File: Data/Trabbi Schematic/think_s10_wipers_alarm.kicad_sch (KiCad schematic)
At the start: 7 parts, among them K1 Wiper Relay R1, K2 Tailgate Release Relay R13, M1 Wiper Motor (E19), M2 Washer Pump (E10), SW1 Wiper Switch (C26), U1 Alarm Control Unit (P4)

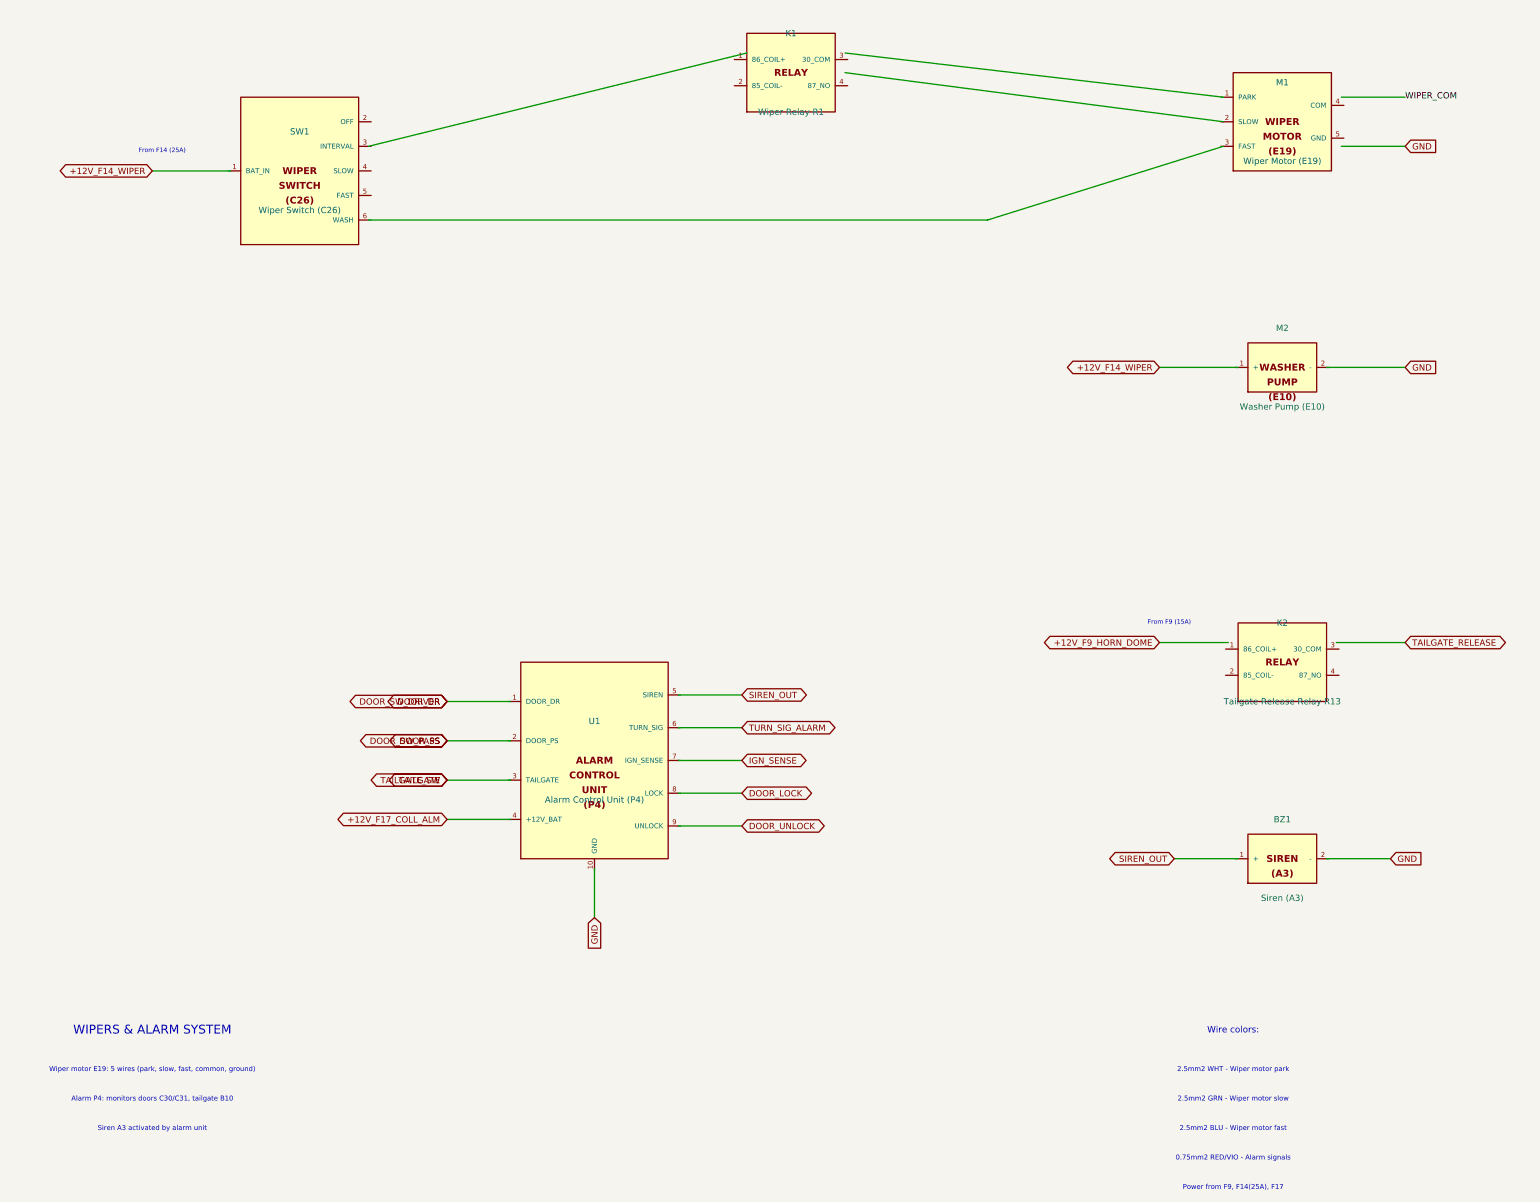
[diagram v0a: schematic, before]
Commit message: Fix wire-to-pin connections: use exact calculated pin positions
Refactored gen_think_complete.py to compute exact pin schematic
coordinates instead of using approximate manual offsets. Added p()
method to Sheet class that transforms symbol-local pin positions to
schematic coordinates. All 232 wire calls across 13 sub-sheet
generators now use p() for pin endpoints, fixing misaligned
connections (previously off by 0.54-10+ units).

Co-Authored-By: Claude Opus 4.6 <noreply@anthropic.com>
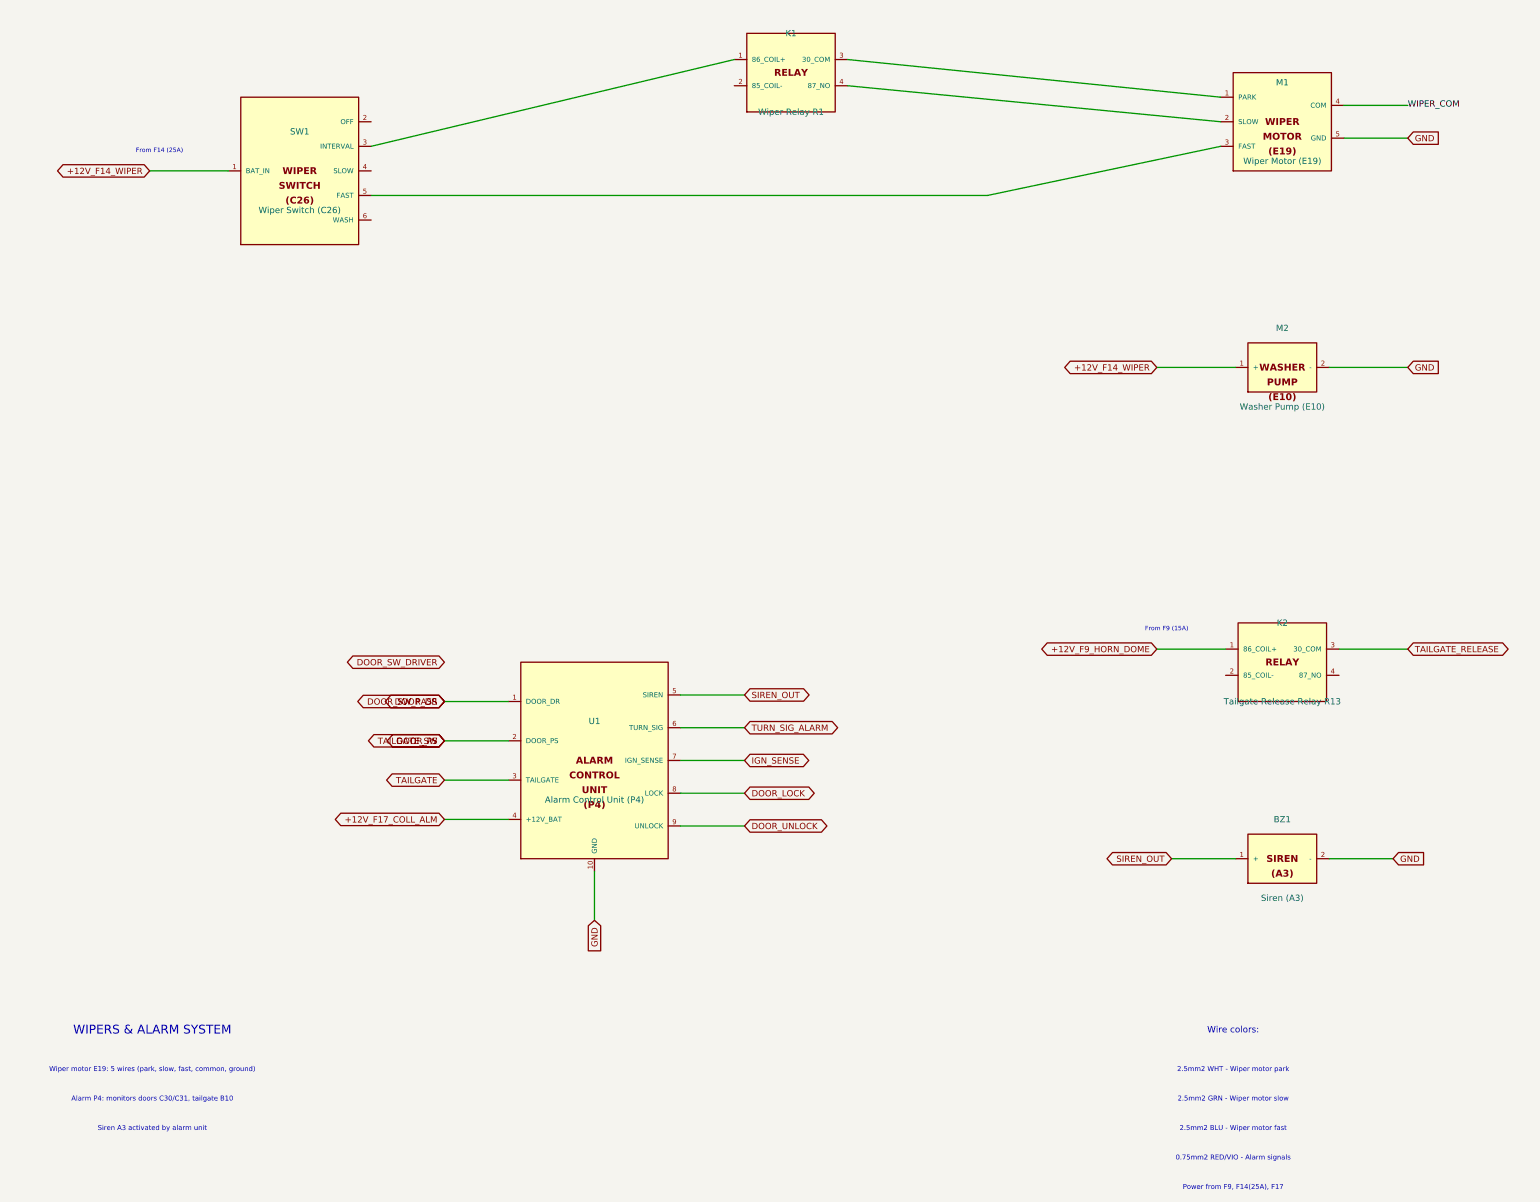
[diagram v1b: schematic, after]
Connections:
- net +12V_F14_WIPER: now also M2.1 (+), SW1.1 (BAT_IN)
- net +12V_F17_COLL_ALM: now also U1.4 (+12V_BAT)
- net +12V_F9_HORN_DOME: now also K2.1 (86_COIL+)
- net DOOR_DR: now also U1.1 (DOOR_DR)
- net DOOR_LOCK: now also U1.8 (LOCK)
- net DOOR_PS: now also U1.2 (DOOR_PS)
- net DOOR_UNLOCK: now also U1.9 (UNLOCK)
- net GND: now also BZ1.2 (-), M1.5 (GND), M2.2 (-), U1.10 (GND)
- net IGN_SENSE: now also U1.7 (IGN_SENSE)
- net SIREN_OUT: now also BZ1.1 (+), U1.5 (SIREN)
- net TAILGATE: now also U1.3 (TAILGATE)
- net TAILGATE_RELEASE: now also K2.3 (30_COM)
- net TURN_SIG_ALARM: now also U1.6 (TURN_SIG)
- net WIPER_COM: now also M1.4 (COM)
- net at SW1.3 (INTERVAL): now also K1.1 (86_COIL+)
- net at SW1.5 (FAST): now also M1.3 (FAST)
- net at K1.3 (30_COM): now also M1.1 (PARK)
- net at K1.4 (87_NO): now also M1.2 (SLOW)

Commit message: Enforce orthogonal routing and 1.27mm grid alignment
- Add _g() grid snap function to Sheet class (rounds all coordinates to nearest 1.27mm)
- Add wire_l() method for L-shaped orthogonal routing (horizontal+vertical segments)
- Apply grid snapping in p(), place(), wire(), label(), glabel(), junction(), no_connect(), defsym()
- Replace all 19 diagonal wire calls with wire_l() across S02, S06, S07, S08, S10, S12, S13
- All wire segments now strictly horizontal or vertical, no diagonals
- All coordinates verified on 1.27mm (50mil) KiCad standard grid

Co-Authored-By: Claude Opus 4.6 <noreply@anthropic.com>
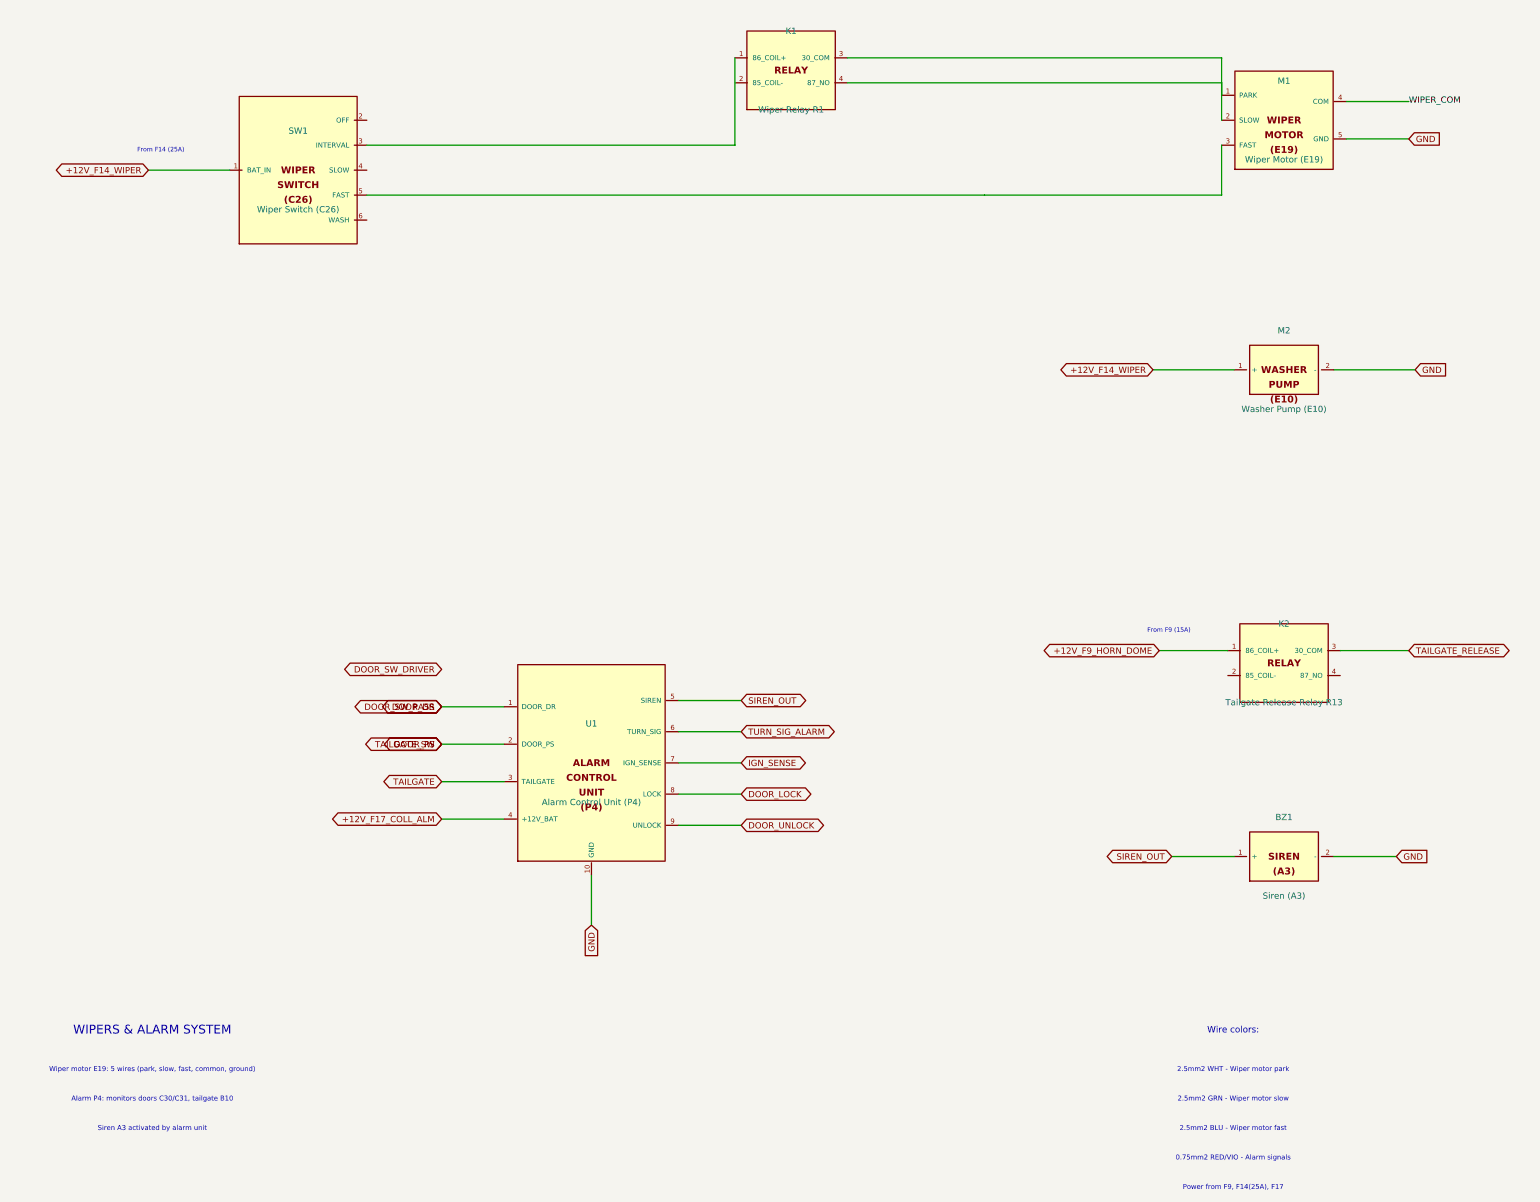
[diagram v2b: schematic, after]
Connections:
- net at K1.3 (30_COM), M1.1 (PARK): now also K1.4 (87_NO), M1.2 (SLOW)

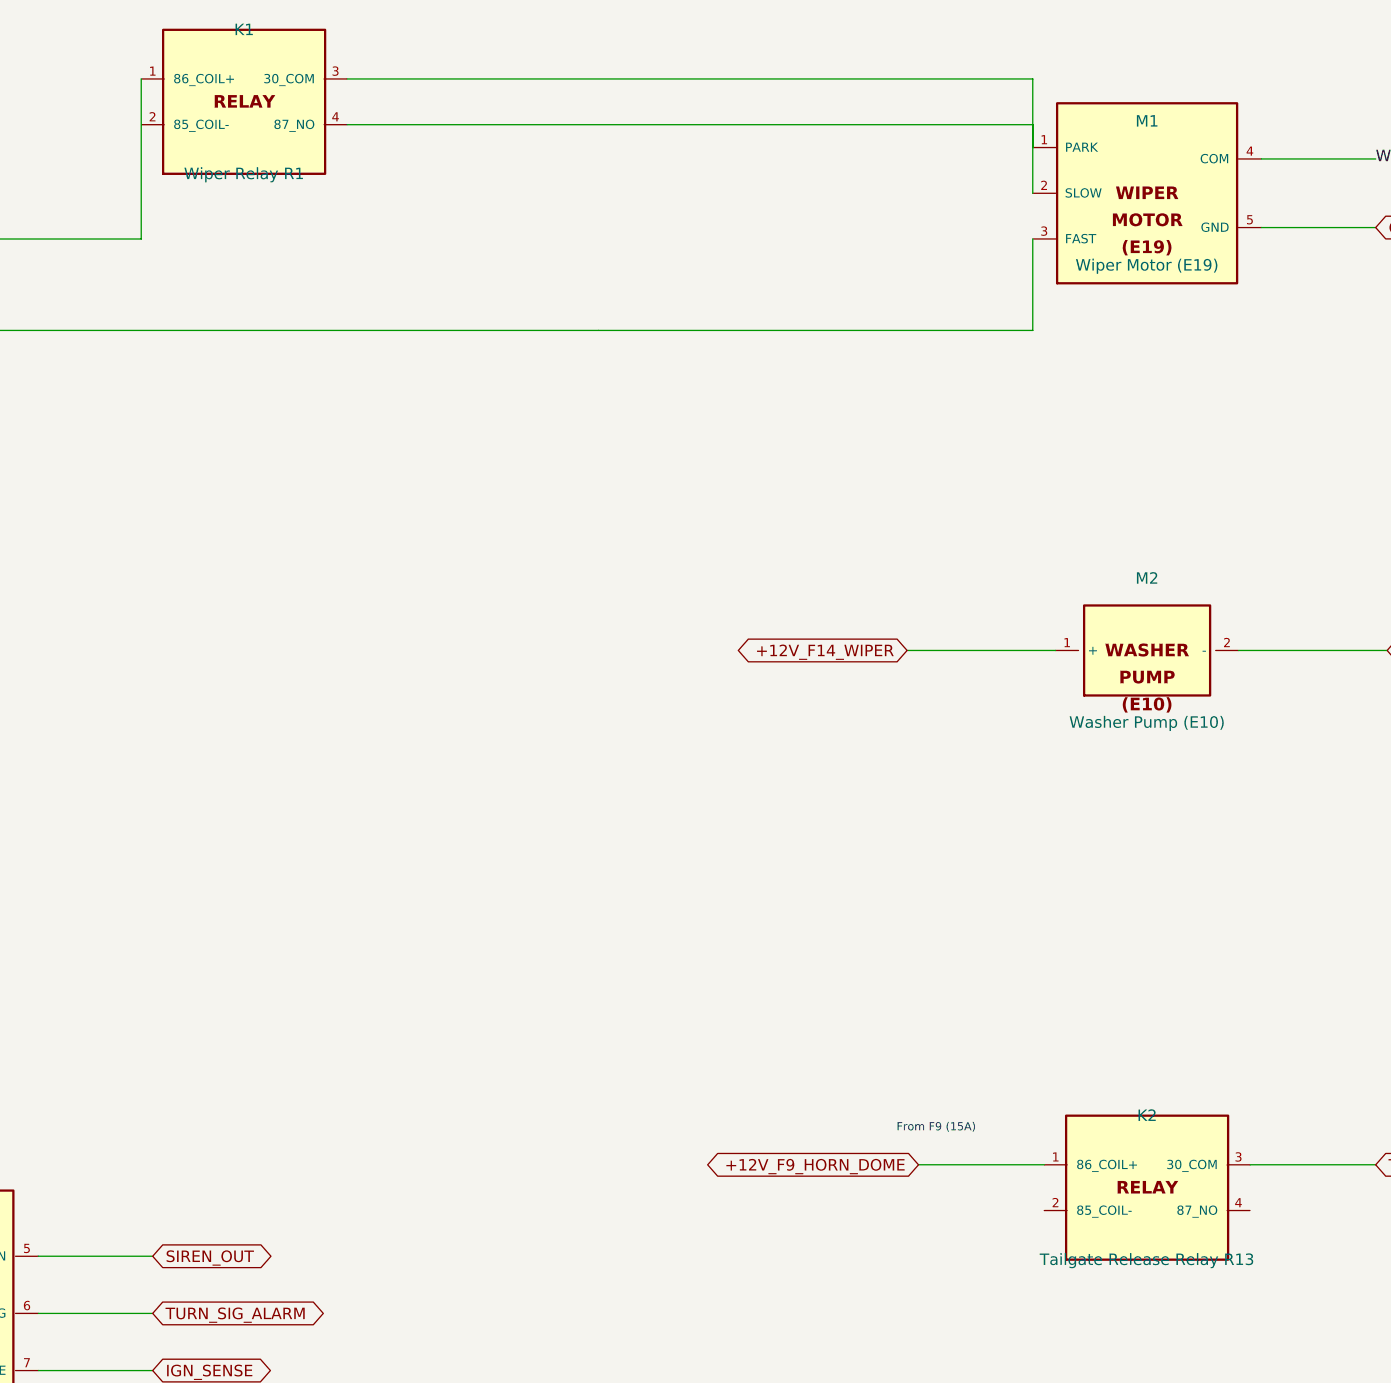
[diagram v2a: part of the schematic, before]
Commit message: Add relay coil/switch graphics, fix label positioning
- Draw coil (inductor arcs) and switch contacts (circles + arm)
  inside RELAY_SPST and RELAY_SPDT symbol bodies
- Add body_gfx parameter to defsym() for custom symbol graphics
- Helper functions: _gfx_polyline, _gfx_arc, _gfx_circle, _relay_gfx
- Fix label offsets: increase from 3-5mm to 10-12mm to avoid
  overlapping pin names (S01 ignition, S02 HV, S05 DCDC, S07 lights)
- Fix S09 turn signal rear labels: add wire stubs (were at 0 offset)
- All 14 schematics regenerated, parentheses balanced, grid OK

Co-Authored-By: Claude Opus 4.6 <noreply@anthropic.com>
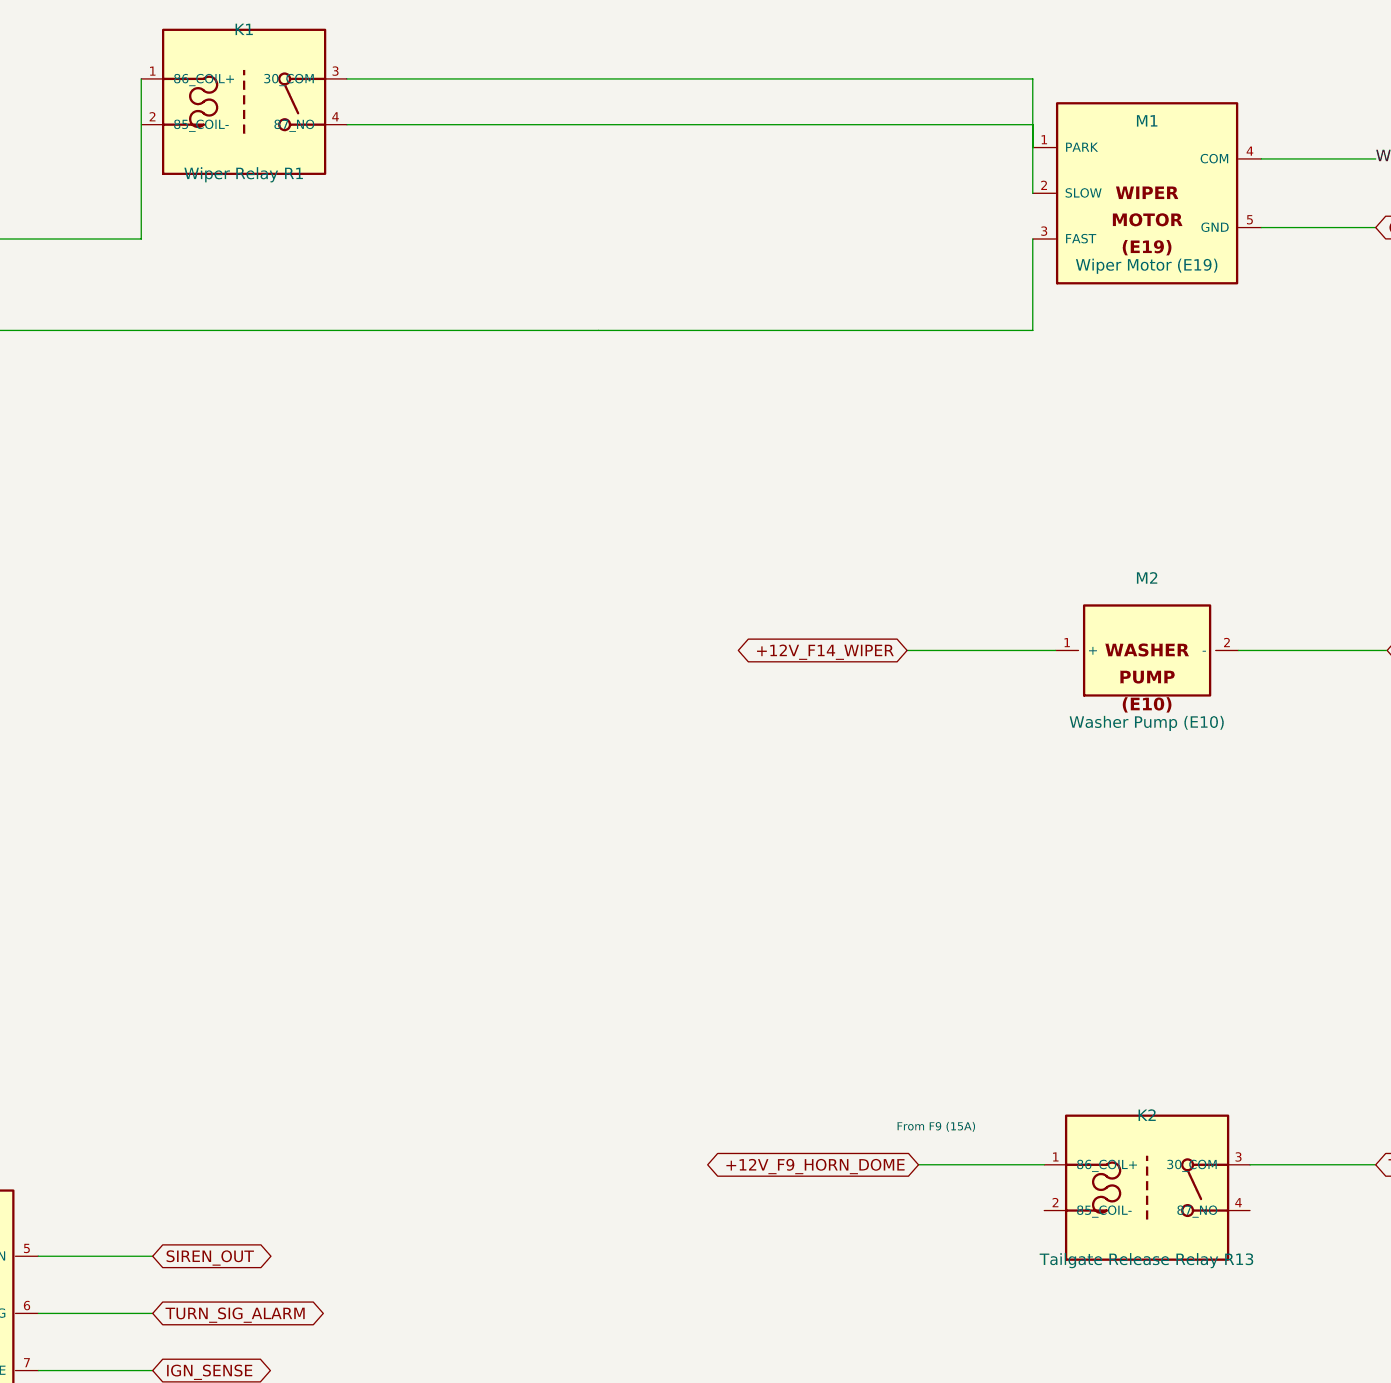
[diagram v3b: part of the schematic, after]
